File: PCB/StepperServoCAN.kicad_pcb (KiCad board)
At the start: 4 copper layers, 56 x 43.2 mm, 144 parts, among them J1 Debug, J2 CAR, J3 Motor, J4 Conn_01x02, Q1 AO3401A, Q2 2N7002, Q3 AO3401A, SW1 Rst, SW2 Fcn>, SW3 Fcn>, U1 AH1806-W, U10 LV2842XLVDDCR, U2 STM32F103CBT6, U3 LMV321, U4 A4950E, U5 A4950E, U6 LMV321, U7 TLE5012B, U8 SN65HVD230, U9 HT75xx-1-SOT89, Y1 16Mhz 9pF

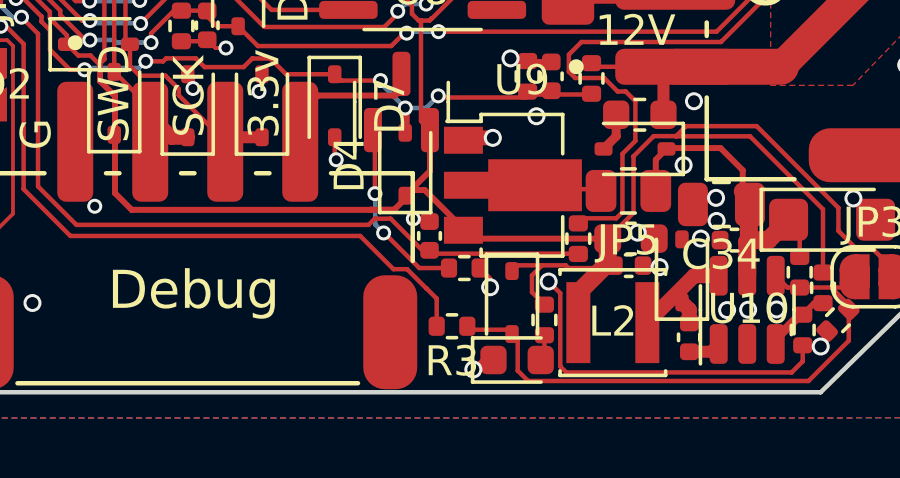
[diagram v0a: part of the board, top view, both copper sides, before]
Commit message: Added undervoltage shutdown filter
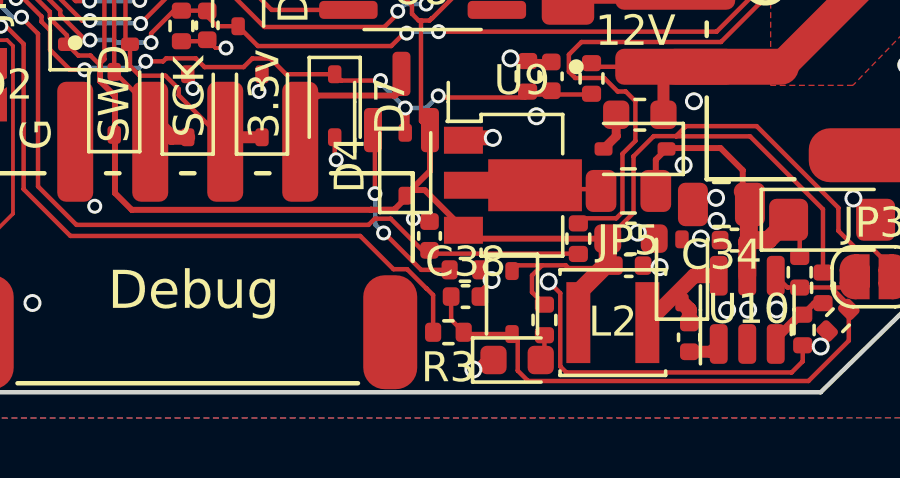
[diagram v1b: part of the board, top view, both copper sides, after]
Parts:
- added C38: 1u, Capacitor_SMD:C_0402_1005Metric, F.Cu at (104.8, 117.2)
- moved R3 0.23 mm to (104.2, 118.4)
- moved R33 0.06 mm to (104.7, 116.3)
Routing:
- net /DCDC 3.3V/Enable: track 19.4 -> 20.8 mm

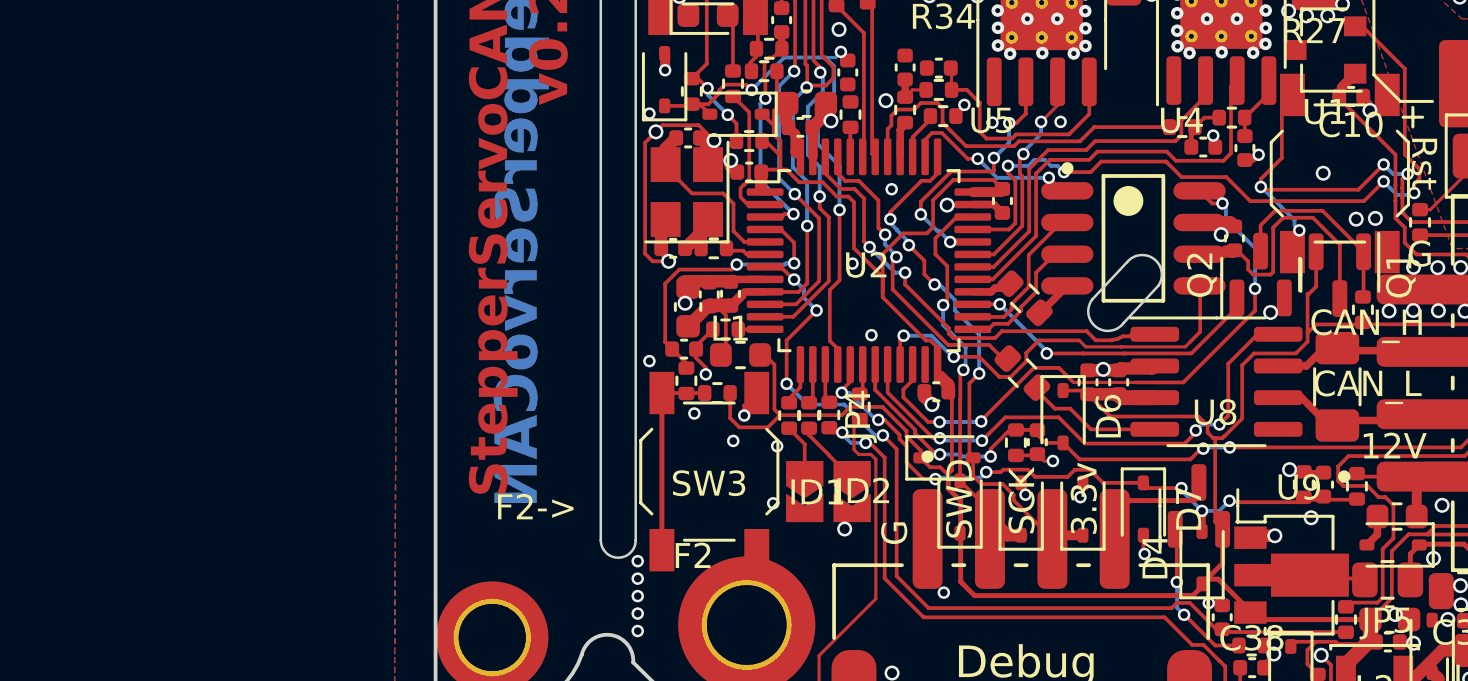
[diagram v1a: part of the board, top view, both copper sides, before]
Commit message: Added test footprint for low power TMAG5170 sensor
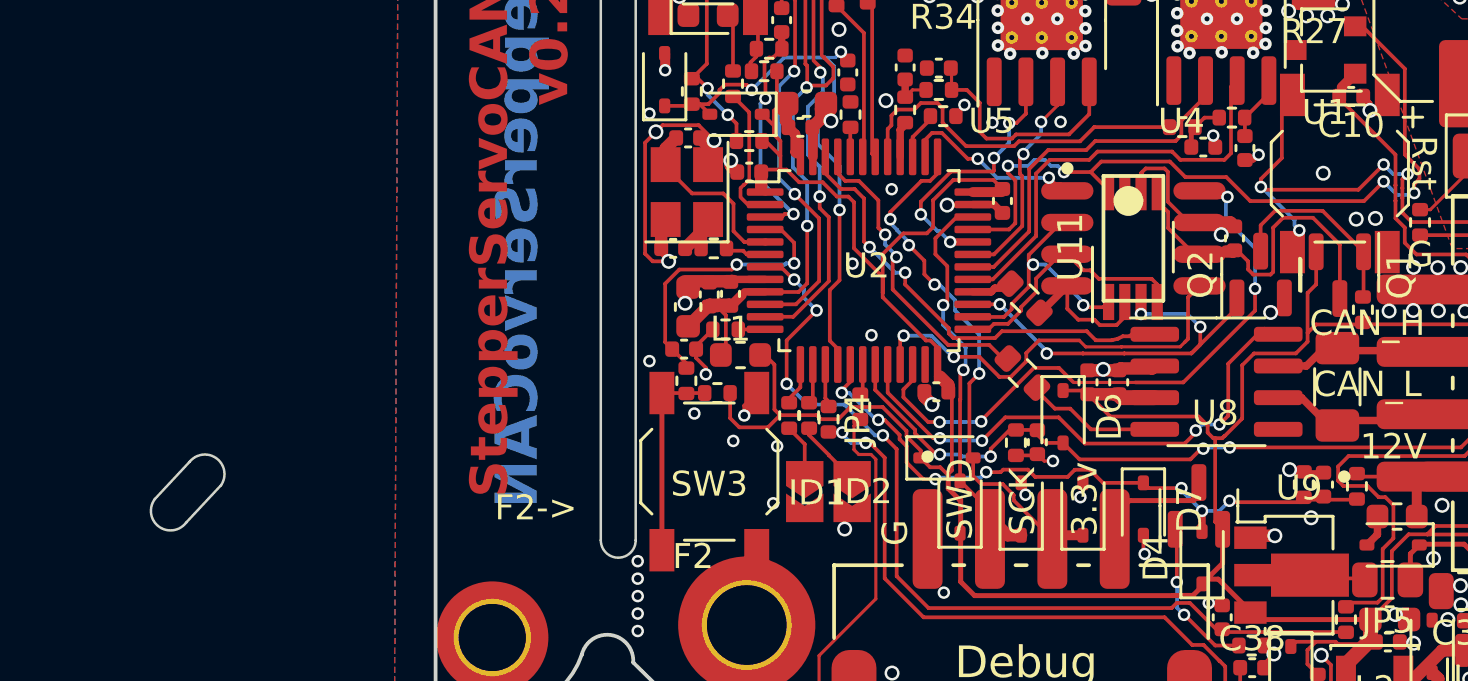
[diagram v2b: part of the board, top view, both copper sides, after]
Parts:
- added U11: TMAG5170-Q1, Package_SO:VSSOP-8_3.0x3.0mm_P0.65mm, F.Cu at (100.0, 100.3)
- moved JP4 0.17 mm to (87.8, 107.2)
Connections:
- net Net-(Q2-G) renamed /AUX_ON
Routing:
- net GND: track 76.9 -> 82.6 mm
- net TLE_CSQ: track 5.58 -> 10.2 mm
- net /AUX_ON: track 12.6 -> 16.9 mm, vias 2 -> 4
- net /TLE_DATA_R: track 1.56 -> 5.79 mm
- net TLE_SCK: track 5.98 -> 10.0 mm, vias 0 -> 2
- net AUX_3.3: track 9.77 -> 13.1 mm
- net HALL: track 30.2 -> 31.3 mm
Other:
- board size 56 x 43.2 mm -> 67.4 x 43.2 mm

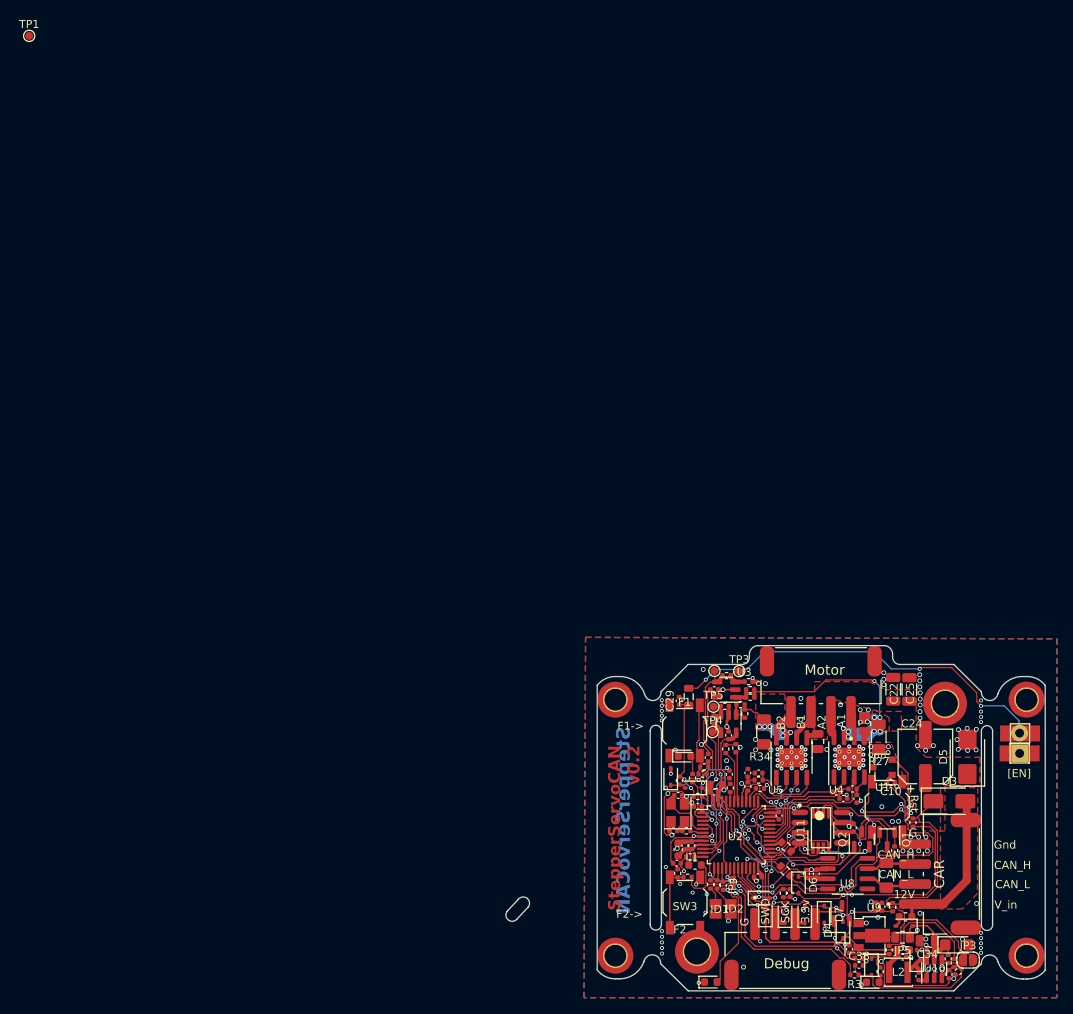
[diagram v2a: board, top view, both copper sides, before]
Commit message: Added UART/I2C aux connector
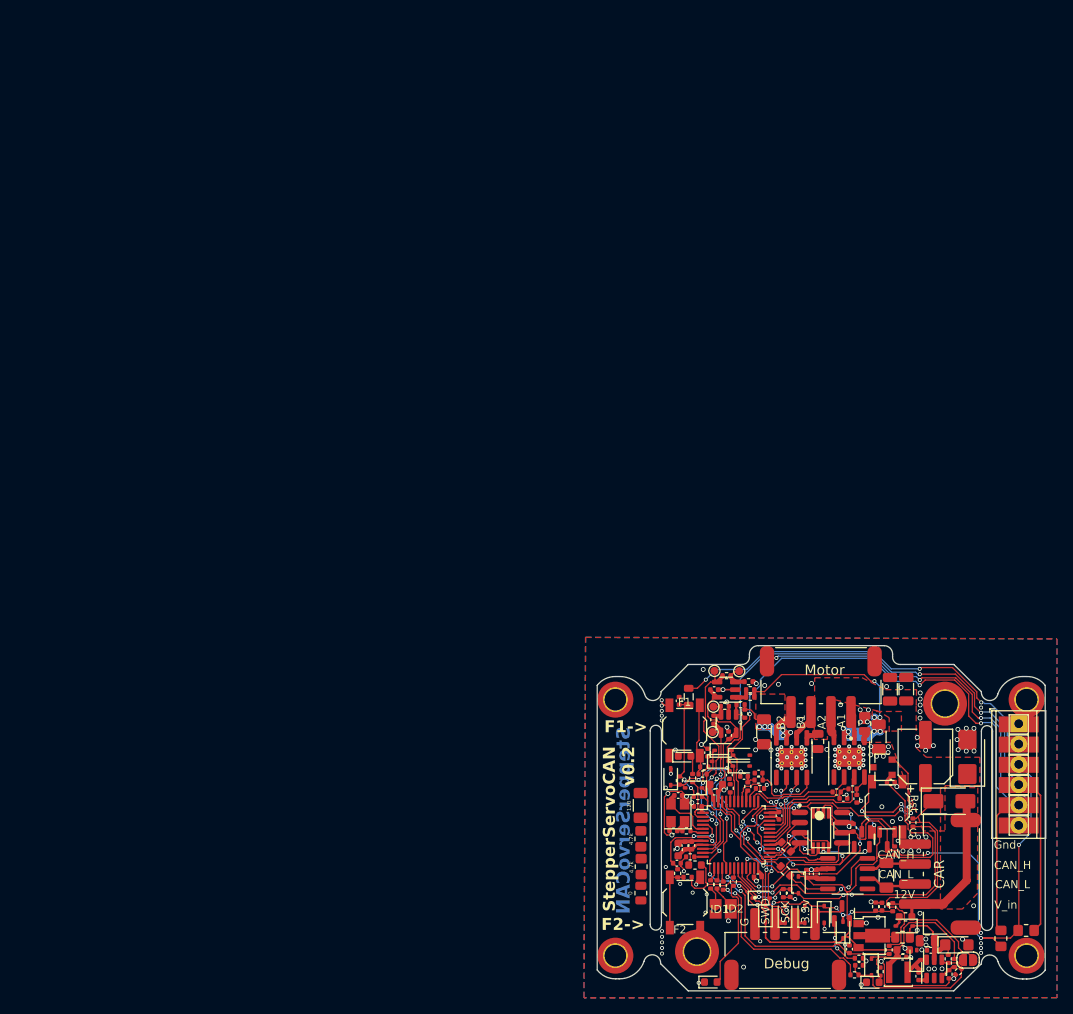
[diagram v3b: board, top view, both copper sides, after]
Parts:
- removed the R28 at (89.3, 90.0)
- removed the R29 at (88.1, 90.2)
- removed the TP1 at (1.02, 1.02)
- added D12: 1N5819WS, Diode_SMD:D_SOD-323, F.Cu at (87.8, 90.3)
- added D13: 1N5819WS, Diode_SMD:D_SOD-323, F.Cu at (87.4, 91.7)
- added D14: 1N5819WS, Diode_SMD:D_SOD-323, F.Cu at (90.1, 90.9)
- added D15: 1N5819WS, Diode_SMD:D_SOD-323, F.Cu at (90.0, 92.3)
- added JP5: 0, Resistor_SMD:R_0805_2012Metric, F.Cu at (77.5, 108.2)
- added R34: 4.7k, Resistor_SMD:R_0805_2012Metric_Pad1.20x1.40mm_HandSolder, F.Cu at (122.5, 113.8)
- added R35: 4.7k, Resistor_SMD:R_0805_2012Metric_Pad1.20x1.40mm_HandSolder, F.Cu at (125.6, 112.8)
- added R39: 4.7k, Resistor_SMD:R_0805_2012Metric_Pad1.20x1.40mm_HandSolder, F.Cu at (77.5, 101.4)
- added R40: 4.7k, Resistor_SMD:R_0805_2012Metric_Pad1.20x1.40mm_HandSolder, F.Cu at (77.5, 104.9)
- added R41: 120, Resistor_SMD:R_1206_3216Metric_Pad1.30x1.75mm_HandSolder, F.Cu at (77.5, 97.2)
- added TP4: WirePad, TestPoint:TestPoint_Pad_2.0x2.0mm, F.Cu at (124.7, 99.7)
- added TP5: WirePad, TestPoint:TestPoint_Pad_2.0x2.0mm, F.Cu at (124.7, 97.2)
- added TP6: WirePad, TestPoint:TestPoint_Pad_2.0x2.0mm, F.Cu at (124.7, 94.7)
- added TP8: WirePad, TestPoint:TestPoint_Pad_2.0x2.0mm, F.Cu at (124.7, 92.1)
- J4: value Conn_01x02 -> Conn_01x06; footprint TerminalBlock_TE-Connectivity:TerminalBlock_TE_282834-2_1x02_P2.54mm_Horizontal -> TerminalBlock_TE-Connectivity:TerminalBlock_TE_282834-6_1x06_P2.54mm_Horizontal; moved to F.Cu
- moved J4 3.71 mm to (124.7, 87.0), turned to -90 degrees
- moved TP10 3.63 mm to (124.7, 87.1)
- moved TP9 1.41 mm to (124.7, 89.6)
- moved C19 0.64 mm to (90.4, 93.6), turned to 180 degrees
- moved C13 0.63 mm to (85.8, 90.6)
- moved C22 0.40 mm to (108.6, 82.7)
- moved C25 0.39 mm to (110.7, 82.7)
- moved C28 0.07 mm to (88.5, 93.4)
- renumbered D12 to D16, D13 to D17, D14 to D18, D15 to D19, D16 to D20, D17 to D21, D18 to D22, J2 to J1, J1 to J2, JP3 to JP1, JP4 to JP2, JP1 to JP3, JP2 to JP4, JP5 to JP6, R30 to R28, R31 to R29, R33 to R30, R32 to R31, R34 to R32, R35 to R33, R37 to R36, R36 to R37, R39 to R42, R40 to R43, R41 to R44, R43 to R46, R44 to R47, R46 to R48, R47 to R49, TP2 to TP1, TP7 to TP10, TP3 to TP2, TP4 to TP3, TP5 to TP7, TP6 to TP9, U9 to U10, U10 to U11, U11 to U8, U8 to U9
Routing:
- net UART_RX: track 6.54 -> 84.3 mm, vias 0 -> 3
- net UART_TX: track 6.30 -> 82.6 mm, vias 0 -> 3
- net AUX_3.3: track 13.1 -> 65.3 mm, vias 0 -> 3
- net GND: track 82.6 -> 126.4 mm, vias 167 -> 162
- net +3.3VA: track 37.1 -> 32.5 mm
- net +3.3V: track 149.9 -> 153.7 mm
- net Net-(U2-PC14): track 9.43 -> 10.1 mm
- net LSS_A_ADC: track 27.1 -> 27.7 mm
- net Net-(J4-Pin_2): track 49.1 -> 49.7 mm
- net LSS_A: track 39.3 -> 39.8 mm
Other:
- board size 67.4 x 43.2 mm -> 56 x 43.2 mm
- board text added: "G En 3.3 RX TX G"
- board text added: "Optional connect"
- board text added: "SDA SCL"
- board text removed: "Optional Enable"

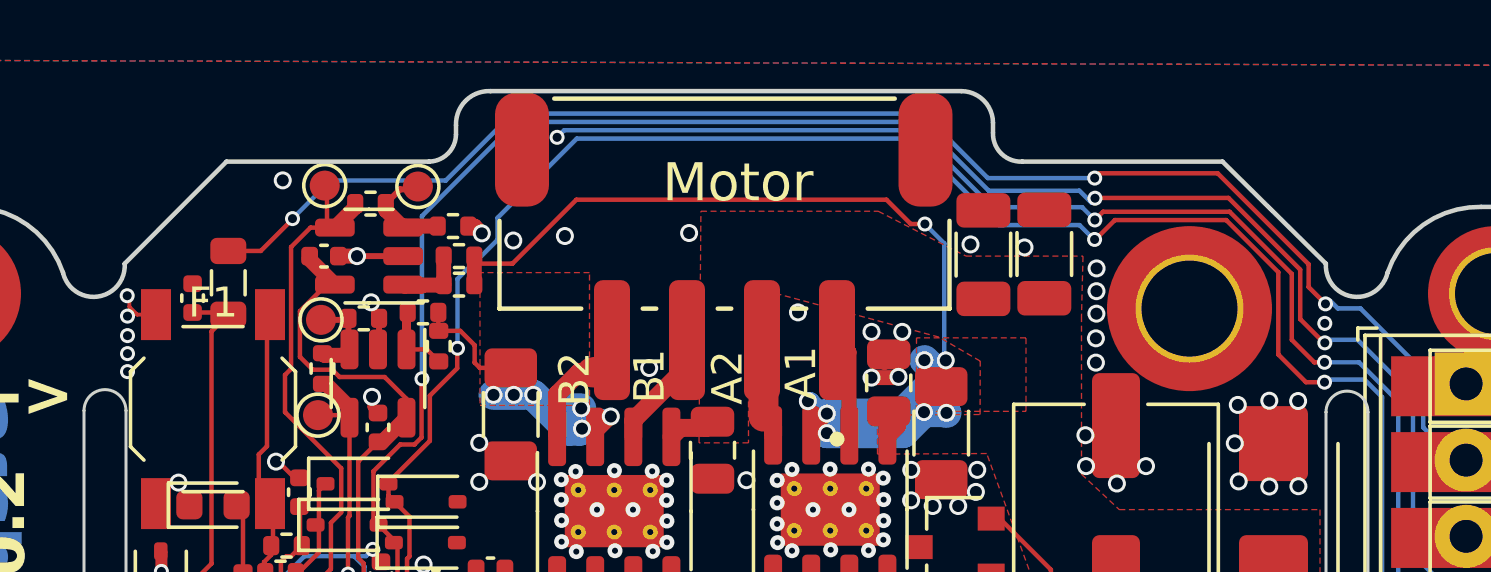
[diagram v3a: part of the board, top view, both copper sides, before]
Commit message: Optimized break in filter
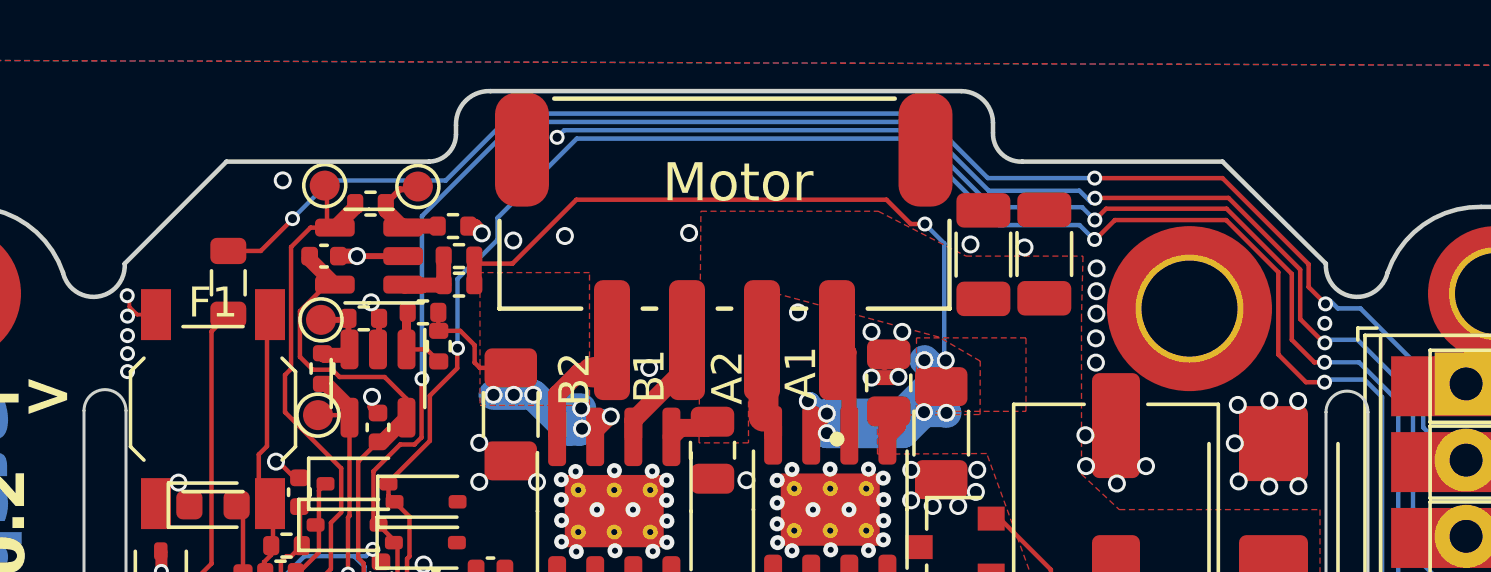
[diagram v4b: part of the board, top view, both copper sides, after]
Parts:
- removed C29: 100n, Capacitor_SMD:C_0402_1005Metric
- C28: value 100n -> 1u
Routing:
- net Net-(FB1-Pad1): track 14.0 -> 12.9 mm

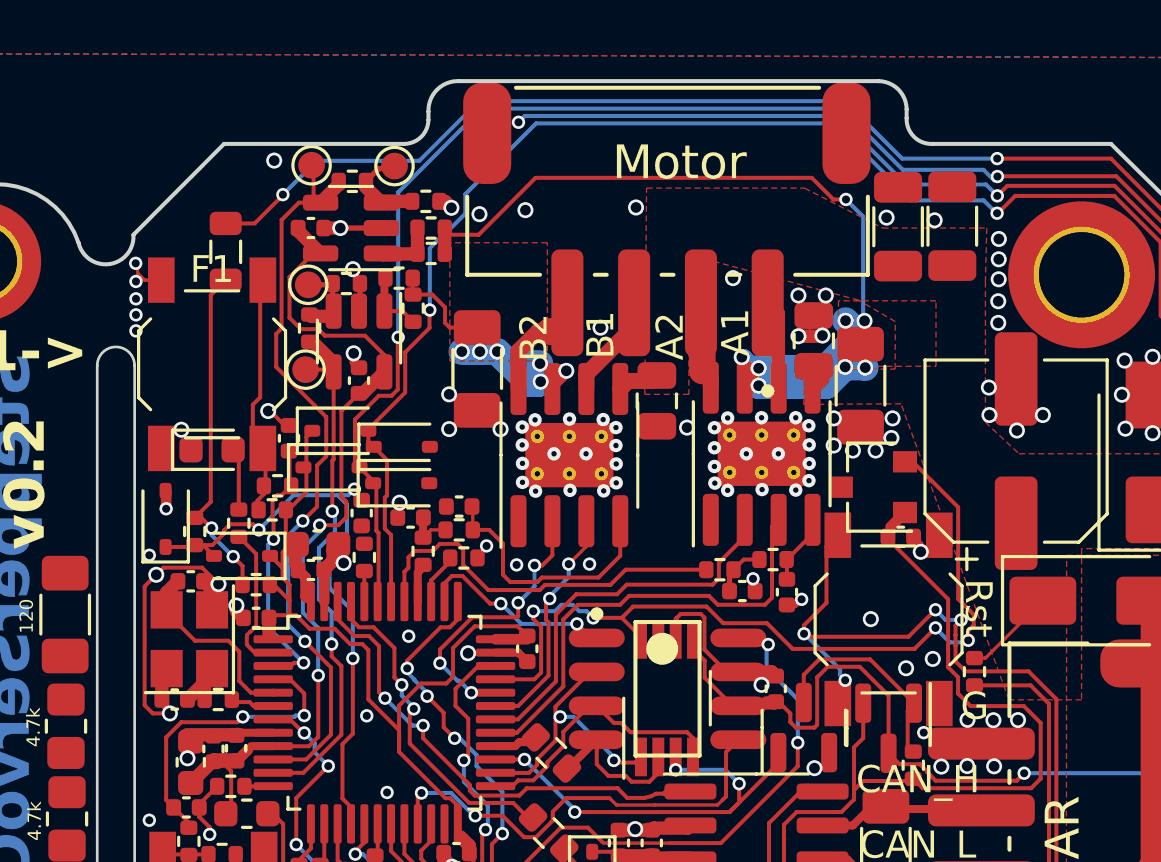
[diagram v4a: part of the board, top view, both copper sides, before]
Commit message: Removed ground loop due to LSS_A for 2 layer board
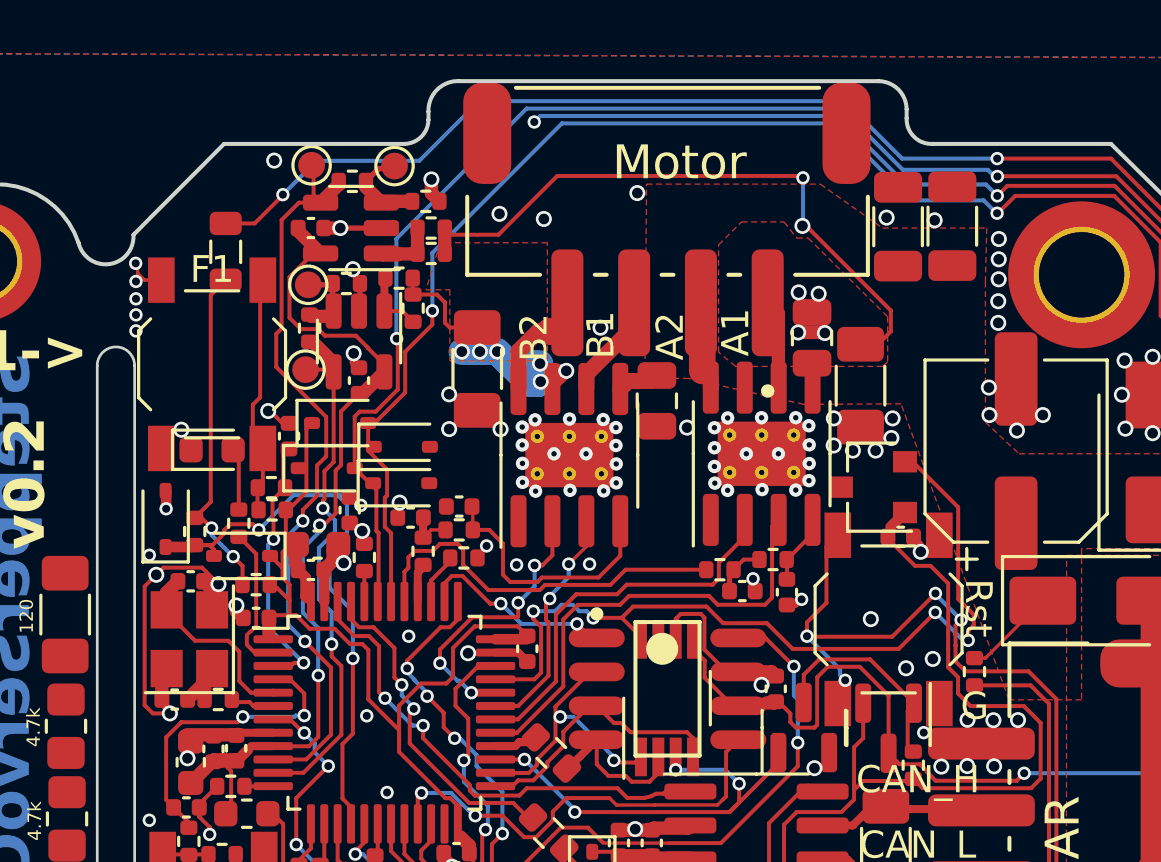
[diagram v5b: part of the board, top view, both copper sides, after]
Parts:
- moved C28 0.46 mm to (88.1, 93.3)
- moved D12 0.29 mm to (87.7, 90.0)
- moved R7 0.24 mm to (85.2, 92.5)
- moved D13 0.18 mm to (87.2, 91.7)
- moved C26 0.13 mm to (105.4, 86.9)
- moved C13 0.08 mm to (85.8, 90.5)
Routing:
- net LSS_A: track 39.8 -> 24.3 mm, vias 8 -> 2
- net VMOT: track 6.08 -> 5.03 mm
- net UART_RX: track 84.3 -> 83.5 mm
- net +3.3VA: track 32.5 -> 31.9 mm
- net +3.3V: track 153.7 -> 154.3 mm
- net GND: track 126.5 -> 125.9 mm
